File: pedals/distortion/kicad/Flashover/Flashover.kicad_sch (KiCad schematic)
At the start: 0 parts

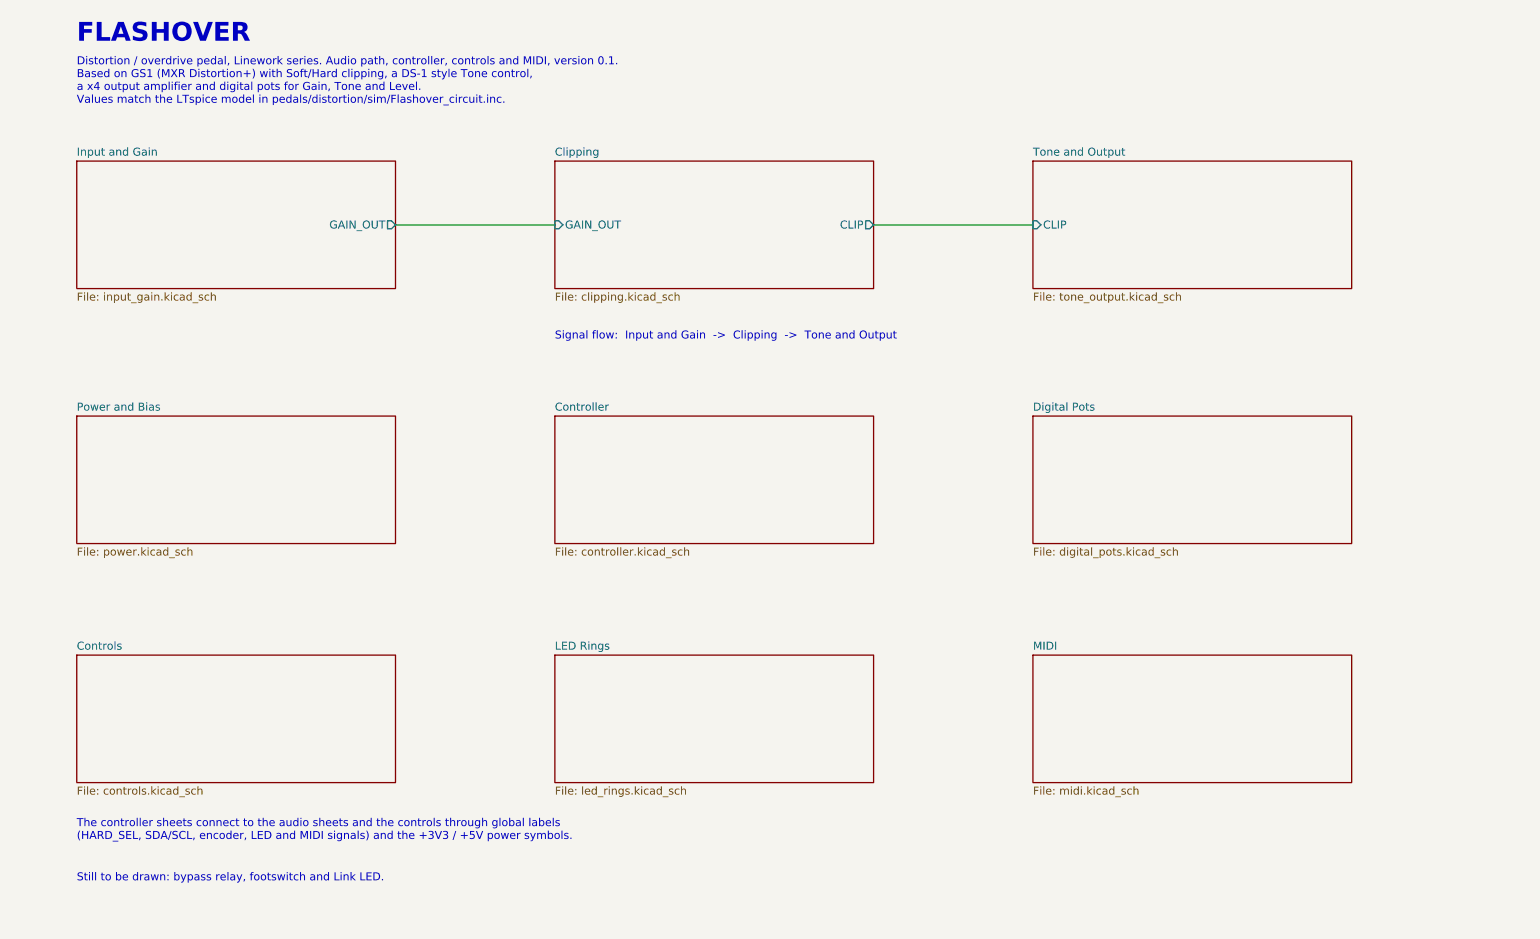
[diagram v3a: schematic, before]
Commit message: Add Flashover bypass sheet; complete schematic
Bypass sheet: fail-safe G6K-2 relay bypass (NC contacts join the jacks
when unpowered), input/output jacks moved here from the audio sheets
(now FX_IN/FX_OUT), relay driver on FX_ON, soft-touch footswitch and
Link LED. Relay coils on K1 and K2 now take +5V on pin 1 (marked +).
Root sheet laid out in four columns. ERC clean.

Co-Authored-By: Claude Opus 5.5 <noreply@anthropic.com>
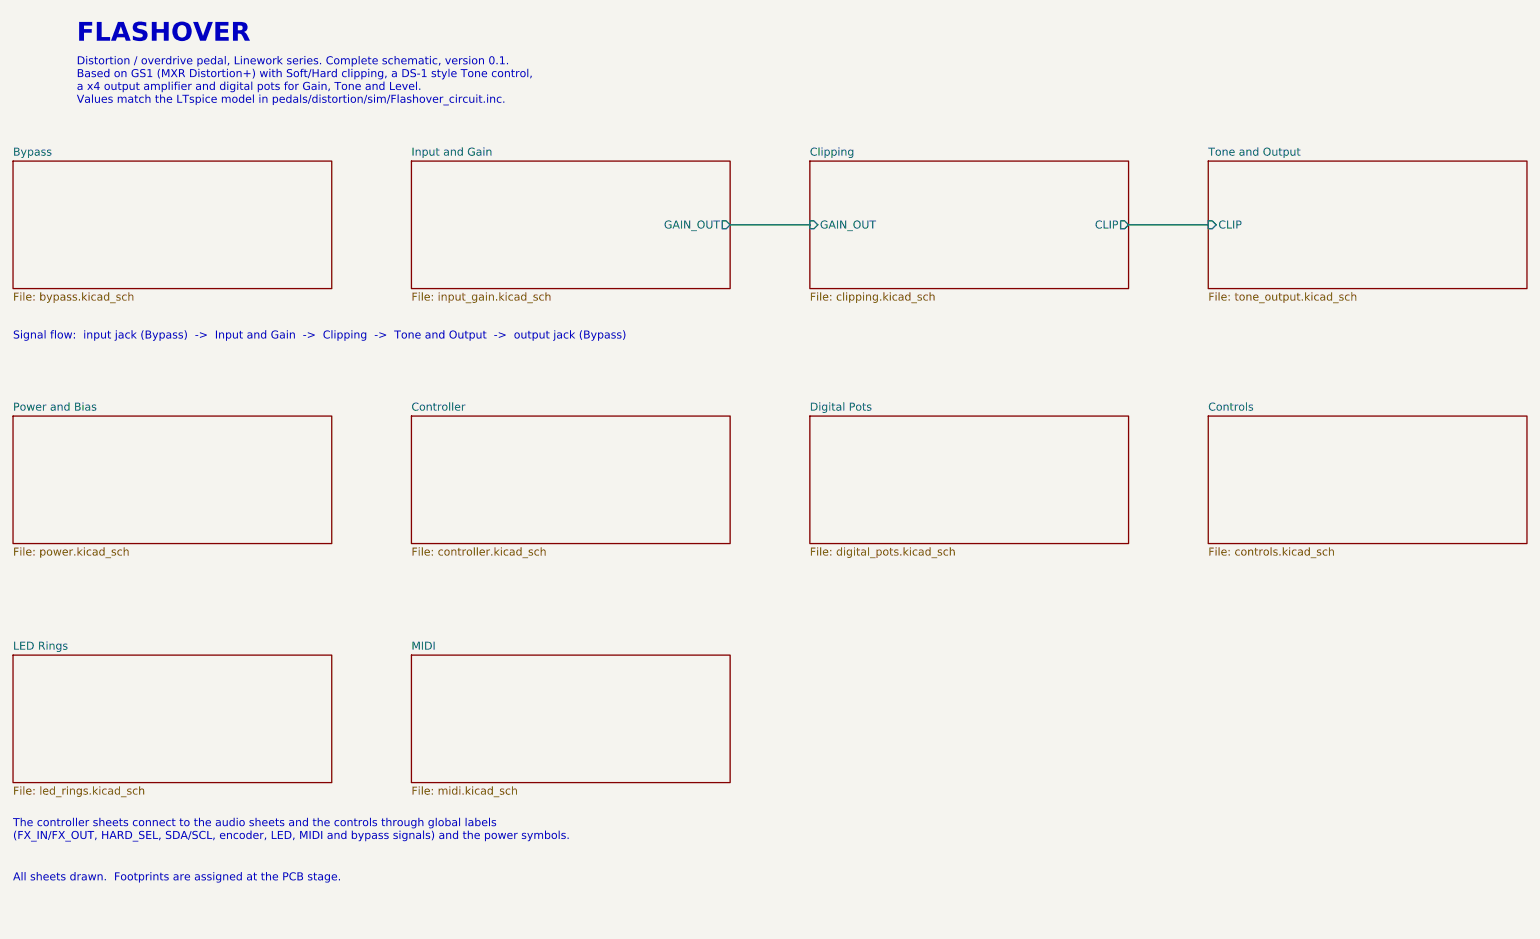
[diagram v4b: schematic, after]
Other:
- added sheet Bypass (bypass.kicad_sch)
- note added: "All sheets drawn. Footprints are assigned at the PCB stage."
- note added: "Distortion / overdrive pedal, Linework series. Complete schematic, version 0.1. Based on GS1 (MXR Distortion+) with Soft/Hard clipping, a DS-1 style Tone control, a x4 output amplifier and digital pots for Gain, Tone and Level. Values match the LTspice model in pedals/distortion/sim/Flashover_circuit.inc."
- note added: "Signal flow: input jack (Bypass) -> Input and Gain -> Clipping -> Tone and Output -> output jack (Bypass)"
- note added: "The controller sheets connect to the audio sheets and the controls through global labels (FX_IN/FX_OUT, HARD_SEL, SDA/SCL, encoder, LED, MIDI and bypass signals) and the power symbols."
- note removed: "Distortion / overdrive pedal, Linework series. Audio path, controller, controls and MIDI, version 0.1. Based on GS1 (MXR Distortion+) with Soft/Hard clipping, a DS-1 style Tone control, a x4 output amplifier and digital pots for Gain, Tone and Level. Values match the LTspice model in pedals/distortion/sim/Flashover_circuit.inc."
- note removed: "Signal flow: Input and Gain -> Clipping -> Tone and Output"
- note removed: "Still to be drawn: bypass relay, footswitch and Link LED."
- note removed: "The controller sheets connect to the audio sheets and the controls through global labels (HARD_SEL, SDA/SCL, encoder, LED and MIDI signals) and the +3V3 / +5V power symbols."
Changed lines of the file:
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@@
 	(wire
 		(pts
-			(xy 91.44 68.58) (xy 116.84 68.58)
+			(xy 144.78 68.58) (xy 157.48 68.58)
 		)
 		(stroke
@@
 	(wire
 		(pts
-			(xy 167.64 68.58) (xy 193.04 68.58)
+			(xy 208.28 68.58) (xy 220.98 68.58)
 		)
 		(stroke
@@
 		(effects (font (size 3 3) (bold yes)) (justify left))
 	)
-	(text "Distortion / overdrive pedal, Linework series. Audio path, controller, controls and MIDI, version 0.1.\nBased on GS1 (MXR Distortion+) with Soft/Hard clipping, a DS-1 style Tone control,\na x4 output amplifier and digital pots for Gain, Tone and Level.\nValues match the LTspice model in pedals/distortion/sim/Flashover_circuit.inc."
+	(text "Distortion / overdrive pedal, Linework series. Complete schematic, version 0.1.\nBased on GS1 (MXR Distortion+) with Soft/Hard clipping, a DS-1 style Tone control,\na x4 output amplifier and digital pots for Gain, Tone and Level.\nValues match the LTspice model in pedals/distortion/sim/Flashover_circuit.inc."
 		(exclude_from_sim no)
 		(at 40.64 45.72 0)
 		(effects (font (size 1.27 1.27)) (justify left))
 	)
-	(text "Signal flow:  Input and Gain  ->  Clipping  ->  Tone and Output"
-		(exclude_from_sim no)
-		(at 116.84 86.36 0)
+	(text "Signal flow:  input jack (Bypass)  ->  Input and Gain  ->  Clipping  ->  Tone and Output  ->  output jack (Bypass)"
+		(exclude_from_sim no)
+		(at 30.48 86.36 0)
 		(effects (font (size 1.27 1.27)) (justify left))
 	)
-	(text "The controller sheets connect to the audio sheets and the controls through global labels\n(HARD_SEL, SDA/SCL, encoder, LED and MIDI signals) and the +3V3 / +5V power symbols."
-		(exclude_from_sim no)
-		(at 40.64 165.1 0)
+	(text "The controller sheets connect to the audio sheets and the controls through global labels\n(FX_IN/FX_OUT, HARD_SEL, SDA/SCL, encoder, LED, MIDI and bypass signals) and the power symbols."
+		(exclude_from_sim no)
+		(at 30.48 165.1 0)
 		(effects (font (size 1.27 1.27)) (justify left))
 	)
-	(text "Still to be drawn: bypass relay, footswitch and Link LED."
-		(exclude_from_sim no)
-		(at 40.64 172.72 0)
+	(text "All sheets drawn.  Footprints are assigned at the PCB stage."
+		(exclude_from_sim no)
+		(at 30.48 172.72 0)
 		(effects (font (size 1.27 1.27)) (justify left))
 	)
 	(sheet
-		(at 40.64 99.06)
+		(at 30.48 99.06)
 		(size 50.8 20.32)
 		(exclude_from_sim no)
@@
 		)
 		(property "Sheetname" "Power and Bias"
-			(at 40.64 98.3484 0)
+			(at 30.48 98.3484 0)
 			(show_name no)
 			(do_not_autoplace no)
@@
 		)
 		(property "Sheetfile" "power.kicad_sch"
-			(at 40.64 119.9646 0)
-			(show_name no)
-			(do_not_autoplace no)
-			(effects (font (size 1.27 1.27)) (justify left top))
-		)
-		(instances
-			(project "Flashover"
-				(path "/6aa723b4-171b-4dbf-8521-b922c86d1498"
+			(at 30.48 119.9646 0)
+			(show_name no)
+			(do_not_autoplace no)
+			(effects (font (size 1.27 1.27)) (justify left top))
+		)
+		(instances
+			(project "Flashover"
+				(path "/d44d1406-41c8-4e08-862e-64ff4a05b8dc"
 					(page "2")
 				)
@@
 	)
 	(sheet
-		(at 40.64 58.42)
+		(at 93.98 58.42)
 		(size 50.8 20.32)
 		(exclude_from_sim no)
@@
 		)
 		(property "Sheetname" "Input and Gain"
-			(at 40.64 57.7084 0)
+			(at 93.98 57.7084 0)
 			(show_name no)
 			(do_not_autoplace no)
@@
 		)
 		(property "Sheetfile" "input_gain.kicad_sch"
-			(at 40.64 79.3246 0)
+			(at 93.98 79.3246 0)
 			(show_name no)
 			(do_not_autoplace no)
@@
 		)
 		(pin "GAIN_OUT" output
-			(at 91.44 68.58 0)
+			(at 144.78 68.58 0)
 			(effects (font (size 1.27 1.27)) (justify right))
 		)
 		(instances
 			(project "Flashover"
-				(path "/6aa723b4-171b-4dbf-8521-b922c86d1498"
+				(path "/d44d1406-41c8-4e08-862e-64ff4a05b8dc"
 					(page "3")
 				)
@@
 	)
 	(sheet
-		(at 116.84 58.42)
+		(at 157.48 58.42)
 		(size 50.8 20.32)
 		(exclude_from_sim no)
@@
 		)
 		(property "Sheetname" "Clipping"
-			(at 116.84 57.7084 0)
+			(at 157.48 57.7084 0)
 			(show_name no)
 			(do_not_autoplace no)
@@
 		)
 		(property "Sheetfile" "clipping.kicad_sch"
-			(at 116.84 79.3246 0)
+			(at 157.48 79.3246 0)
 			(show_name no)
 			(do_not_autoplace no)
@@
 		)
 		(pin "GAIN_OUT" input
-			(at 116.84 68.58 180)
+			(at 157.48 68.58 180)
 			(effects (font (size 1.27 1.27)) (justify left))
 		)
 		(pin "CLIP" output
-			(at 167.64 68.58 0)
+			(at 208.28 68.58 0)
 			(effects (font (size 1.27 1.27)) (justify right))
 		)
 		(instances
 			(project "Flashover"
-				(path "/6aa723b4-171b-4dbf-8521-b922c86d1498"
+				(path "/d44d1406-41c8-4e08-862e-64ff4a05b8dc"
 					(page "4")
 				)
@@
 	)
 	(sheet
-		(at 193.04 58.42)
+		(at 220.98 58.42)
 		(size 50.8 20.32)
 		(exclude_from_sim no)
@@
 		)
 		(property "Sheetname" "Tone and Output"
-			(at 193.04 57.7084 0)
+			(at 220.98 57.7084 0)
 			(show_name no)
 			(do_not_autoplace no)
@@
 		)
 		(property "Sheetfile" "tone_output.kicad_sch"
-			(at 193.04 79.3246 0)
+			(at 220.98 79.3246 0)
 			(show_name no)
 			(do_not_autoplace no)
@@
 		)
 		(pin "CLIP" input
-			(at 193.04 68.58 180)
+			(at 220.98 68.58 180)
 			(effects (font (size 1.27 1.27)) (justify left))
 		)
 		(instances
 			(project "Flashover"
-				(path "/6aa723b4-171b-4dbf-8521-b922c86d1498"
+				(path "/d44d1406-41c8-4e08-862e-64ff4a05b8dc"
 					(page "5")
 				)
@@
 	)
 	(sheet
-		(at 116.84 99.06)
+		(at 93.98 99.06)
 		(size 50.8 20.32)
 		(exclude_from_sim no)
@@
 		)
 		(property "Sheetname" "Controller"
-			(at 116.84 98.3484 0)
+			(at 93.98 98.3484 0)
 			(show_name no)
 			(do_not_autoplace no)
@@
 		)
 		(property "Sheetfile" "controller.kicad_sch"
-			(at 116.84 119.9646 0)
-			(show_name no)
-			(do_not_autoplace no)
-			(effects (font (size 1.27 1.27)) (justify left top))
-		)
-		(instances
-			(project "Flashover"
-				(path "/6aa723b4-171b-4dbf-8521-b922c86d1498"
+			(at 93.98 119.9646 0)
+			(show_name no)
+			(do_not_autoplace no)
+			(effects (font (size 1.27 1.27)) (justify left top))
+		)
+		(instances
+			(project "Flashover"
+				(path "/d44d1406-41c8-4e08-862e-64ff4a05b8dc"
 					(page "6")
 				)
@@
 	)
 	(sheet
-		(at 193.04 99.06)
+		(at 157.48 99.06)
 		(size 50.8 20.32)
 		(exclude_from_sim no)
@@
 		)
 		(property "Sheetname" "Digital Pots"
-			(at 193.04 98.3484 0)
+			(at 157.48 98.3484 0)
 			(show_name no)
 			(do_not_autoplace no)
@@
 		)
 		(property "Sheetfile" "digital_pots.kicad_sch"
-			(at 193.04 119.9646 0)
-			(show_name no)
-			(do_not_autoplace no)
-			(effects (font (size 1.27 1.27)) (justify left top))
-		)
-		(instances
-			(project "Flashover"
-				(path "/6aa723b4-171b-4dbf-8521-b922c86d1498"
+			(at 157.48 119.9646 0)
+			(show_name no)
+			(do_not_autoplace no)
+			(effects (font (size 1.27 1.27)) (justify left top))
+		)
+		(instances
+			(project "Flashover"
+				(path "/d44d1406-41c8-4e08-862e-64ff4a05b8dc"
 					(page "7")
 				)
@@
 	)
 	(sheet
-		(at 40.64 137.16)
+		(at 220.98 99.06)
 		(size 50.8 20.32)
 		(exclude_from_sim no)
@@
 		)
 		(property "Sheetname" "Controls"
-			(at 40.64 136.4484 0)
+			(at 220.98 98.3484 0)
 			(show_name no)
 			(do_not_autoplace no)
@@
 		)
 		(property "Sheetfile" "controls.kicad_sch"
-			(at 40.64 158.0646 0)
-			(show_name no)
-			(do_not_autoplace no)
-			(effects (font (size 1.27 1.27)) (justify left top))
-		)
-		(instances
-			(project "Flashover"
-				(path "/6aa723b4-171b-4dbf-8521-b922c86d1498"
+			(at 220.98 119.9646 0)
+			(show_name no)
+			(do_not_autoplace no)
+			(effects (font (size 1.27 1.27)) (justify left top))
+		)
+		(instances
+			(project "Flashover"
+				(path "/d44d1406-41c8-4e08-862e-64ff4a05b8dc"
 					(page "8")
 				)
@@
 	)
 	(sheet
-		(at 116.84 137.16)
+		(at 30.48 137.16)
 		(size 50.8 20.32)
 		(exclude_from_sim no)
@@
 		)
 		(property "Sheetname" "LED Rings"
-			(at 116.84 136.4484 0)
+			(at 30.48 136.4484 0)
 			(show_name no)
 			(do_not_autoplace no)
@@
 		)
 		(property "Sheetfile" "led_rings.kicad_sch"
-			(at 116.84 158.0646 0)
-			(show_name no)
-			(do_not_autoplace no)
-			(effects (font (size 1.27 1.27)) (justify left top))
-		)
-		(instances
-			(project "Flashover"
-				(path "/6aa723b4-171b-4dbf-8521-b922c86d1498"
+			(at 30.48 158.0646 0)
+			(show_name no)
+			(do_not_autoplace no)
+			(effects (font (size 1.27 1.27)) (justify left top))
+		)
+		(instances
+			(project "Flashover"
+				(path "/d44d1406-41c8-4e08-862e-64ff4a05b8dc"
 					(page "9")
 				)
@@
 	)
 	(sheet
-		(at 193.04 137.16)
+		(at 93.98 137.16)
 		(size 50.8 20.32)
 		(exclude_from_sim no)
@@
 		)
 		(property "Sheetname" "MIDI"
-			(at 193.04 136.4484 0)
+			(at 93.98 136.4484 0)
 			(show_name no)
 			(do_not_autoplace no)
@@
 		)
 		(property "Sheetfile" "midi.kicad_sch"
-			(at 193.04 158.0646 0)
-			(show_name no)
-			(do_not_autoplace no)
-			(effects (font (size 1.27 1.27)) (justify left top))
-		)
-		(instances
-			(project "Flashover"
-				(path "/6aa723b4-171b-4dbf-8521-b922c86d1498"
+			(at 93.98 158.0646 0)
+			(show_name no)
+			(do_not_autoplace no)
+			(effects (font (size 1.27 1.27)) (justify left top))
+		)
+		(instances
+			(project "Flashover"
+				(path "/d44d1406-41c8-4e08-862e-64ff4a05b8dc"
 					(page "10")
 				)
 			)
+		)
+	)
+	(sheet
+		(at 30.48 58.42)
+		(size 50.8 20.32)
+		(exclude_from_sim no)
+		(in_bom yes)
+		(on_board yes)
+		(dnp no)
+		(fields_autoplaced yes)
+		(stroke
+			(width 0.1524)
+			(type solid)
+		)
+		(fill
+			(color 0 0 0 0.0000)
+		)
+		(property "Sheetname" "Bypass"
+			(at 30.48 57.7084 0)
+			(show_name no)
+			(do_not_autoplace no)
+			(effects (font (size 1.27 1.27)) (justify left bottom))
+		)
+		(property "Sheetfile" "bypass.kicad_sch"
+			(at 30.48 79.3246 0)
+			(show_name no)
+			(do_not_autoplace no)
+			(effects (font (size 1.27 1.27)) (justify left top))
+		)
+		(instances
+			(project "Flashover"
+				(path "/d44d1406-41c8-4e08-862e-64ff4a05b8dc"
+					(page "11")
+				)
+			)

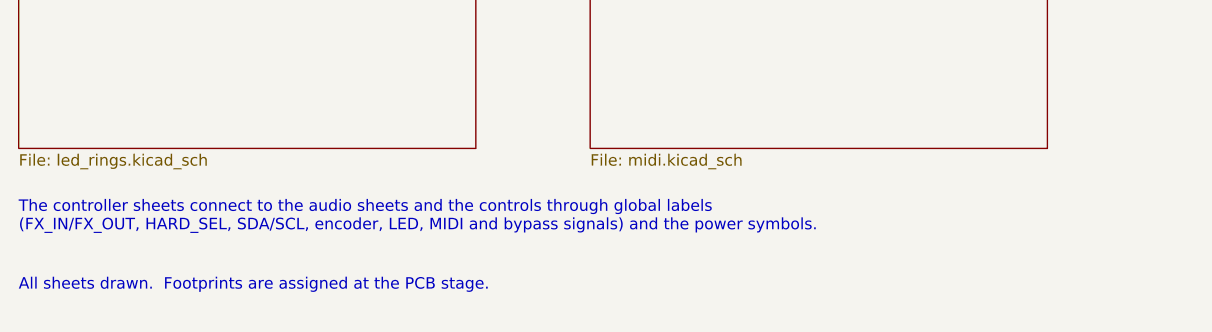
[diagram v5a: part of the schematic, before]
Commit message: Assign Flashover footprints
Surface-mount for assembly; through-hole for jacks, encoders, panel LEDs,
the Soft/Hard button, the TO-220 regulator and the germanium diodes.
Q1/Q2 use the MMBT3904 symbol, 1N4148 -> 1N4148W, 1N5817 -> SS14.

Co-Authored-By: Claude Opus 5.5 <noreply@anthropic.com>
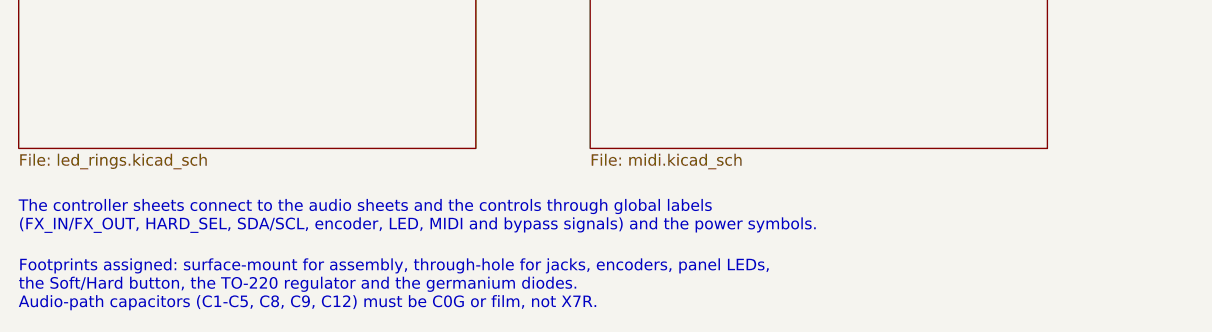
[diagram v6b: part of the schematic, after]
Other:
- note added: "Footprints assigned: surface-mount for assembly, through-hole for jacks, encoders, panel LEDs, the Soft/Hard button, the TO-220 regulator and the germanium diodes. Audio-path capacitors (C1-C5, C8, C9, C12) must be C0G or film, not X7R."
- note removed: "All sheets drawn. Footprints are assigned at the PCB stage."
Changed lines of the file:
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@@
 		(effects (font (size 1.27 1.27)) (justify left))
 	)
-	(text "All sheets drawn.  Footprints are assigned at the PCB stage."
+	(text "Footprints assigned: surface-mount for assembly, through-hole for jacks, encoders, panel LEDs,\nthe Soft/Hard button, the TO-220 regulator and the germanium diodes.\nAudio-path capacitors (C1-C5, C8, C9, C12) must be C0G or film, not X7R."
 		(exclude_from_sim no)
 		(at 30.48 172.72 0)
@@
 		(instances
 			(project "Flashover"
-				(path "/d341370c-bf24-48b8-b9fb-db9600491445"
+				(path "/872055d3-e01a-4a82-8c05-28c93674a700"
 					(page "2")
 				)
@@
 		(instances
 			(project "Flashover"
-				(path "/d341370c-bf24-48b8-b9fb-db9600491445"
+				(path "/872055d3-e01a-4a82-8c05-28c93674a700"
 					(page "3")
 				)
@@
 		(instances
 			(project "Flashover"
-				(path "/d341370c-bf24-48b8-b9fb-db9600491445"
+				(path "/872055d3-e01a-4a82-8c05-28c93674a700"
 					(page "4")
 				)
@@
 		(instances
 			(project "Flashover"
-				(path "/d341370c-bf24-48b8-b9fb-db9600491445"
+				(path "/872055d3-e01a-4a82-8c05-28c93674a700"
 					(page "5")
 				)
@@
 		(instances
 			(project "Flashover"
-				(path "/d341370c-bf24-48b8-b9fb-db9600491445"
+				(path "/872055d3-e01a-4a82-8c05-28c93674a700"
 					(page "6")
 				)
@@
 		(instances
 			(project "Flashover"
-				(path "/d341370c-bf24-48b8-b9fb-db9600491445"
+				(path "/872055d3-e01a-4a82-8c05-28c93674a700"
 					(page "7")
 				)
@@
 		(instances
 			(project "Flashover"
-				(path "/d341370c-bf24-48b8-b9fb-db9600491445"
+				(path "/872055d3-e01a-4a82-8c05-28c93674a700"
 					(page "8")
 				)
@@
 		(instances
 			(project "Flashover"
-				(path "/d341370c-bf24-48b8-b9fb-db9600491445"
+				(path "/872055d3-e01a-4a82-8c05-28c93674a700"
 					(page "9")
 				)
@@
 		(instances
 			(project "Flashover"
-				(path "/d341370c-bf24-48b8-b9fb-db9600491445"
+				(path "/872055d3-e01a-4a82-8c05-28c93674a700"
 					(page "10")
 				)
@@
 		(instances
 			(project "Flashover"
-				(path "/d341370c-bf24-48b8-b9fb-db9600491445"
+				(path "/872055d3-e01a-4a82-8c05-28c93674a700"
 					(page "11")
 				)
